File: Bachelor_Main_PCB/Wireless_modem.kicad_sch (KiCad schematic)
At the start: 59 parts, among them J13 CONMHF1-SMD-G-T, J14 CONMHF1-SMD-G-T, J21 CONMHF1-SMD-G-T, J25 M20-9990245, P1 SF70S006VBAR2000, Q10 NX3008NBKW, Q11 SSM3J358R,LF, Q12 NX3008NBKW, Q5 NX3008NBKW, Q6 NX3008NBKW, Q7 NX3008NBKW, Q8 NX3008NBKW, Q9 NX3008NBKW, U6 ESD7004MUTAG, U7 RC7620_1104627

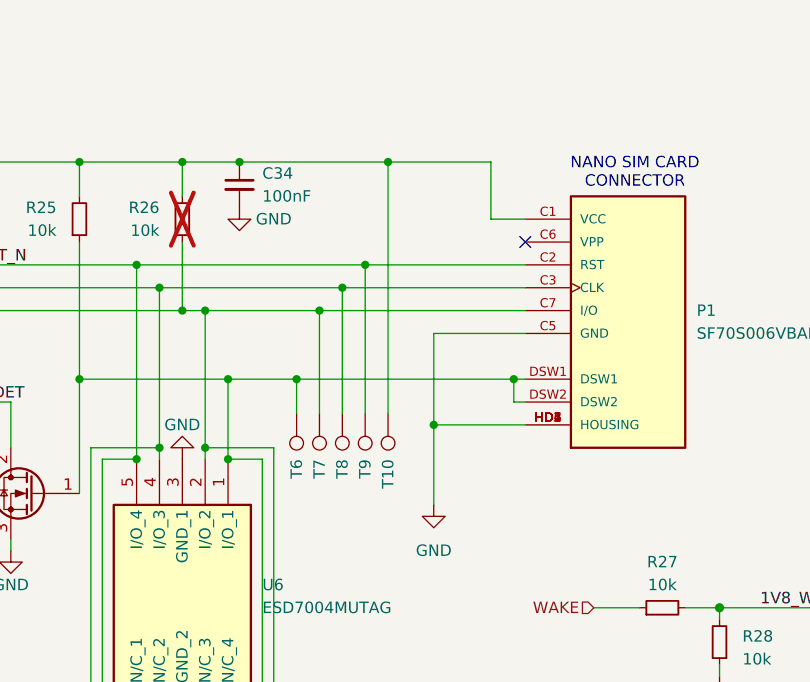
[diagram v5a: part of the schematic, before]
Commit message: arrange SIM card components. Fix DSW1 and DSW2 circuit.
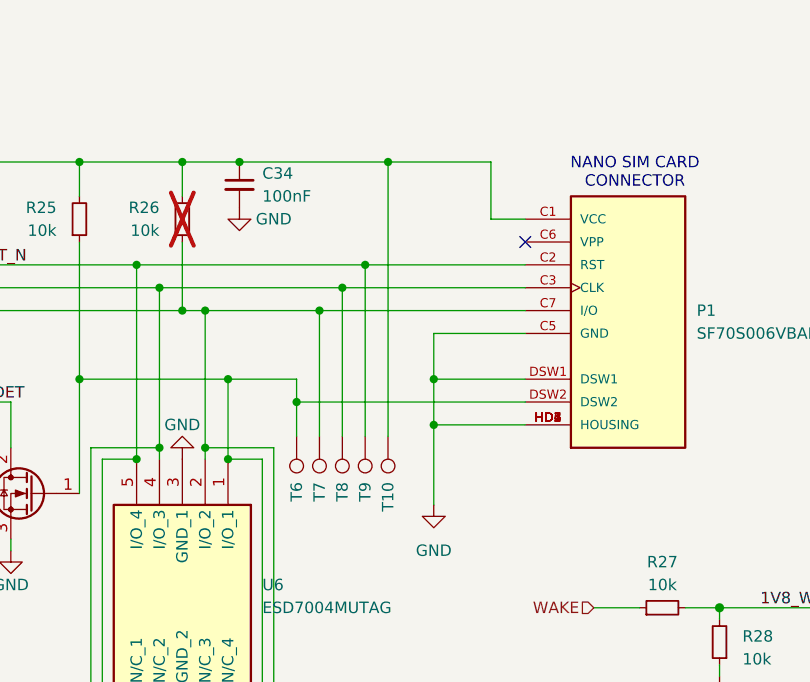
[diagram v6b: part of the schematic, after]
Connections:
- net GND: now also P1.DSW1
- net at P1.DSW2, Q5.1 (G), R25.1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: no longer P1.DSW1
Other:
- moved on the sheet: T10, T6, T7, T8, T9

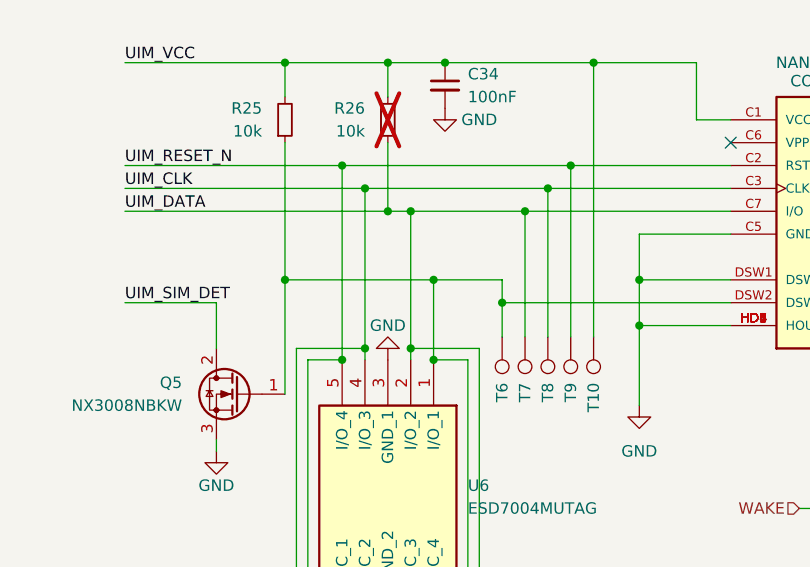
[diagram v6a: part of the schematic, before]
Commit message: arrange Modem mosfets
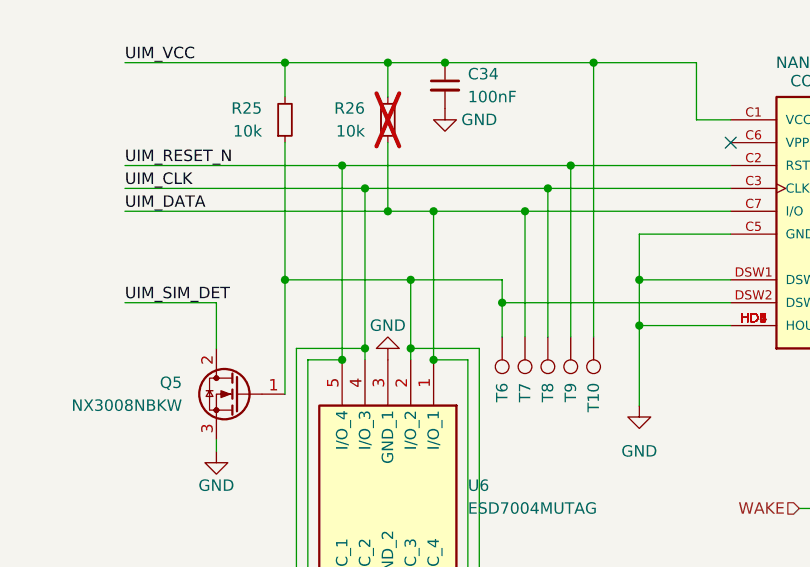
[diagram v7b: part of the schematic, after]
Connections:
- net UIM_DATA: now also U6.1 (I/O_1), U6.10 (N/C_4); no longer U6.2 (I/O_2), U6.9 (N/C_3)
- net at P1.DSW2, Q5.1 (G), R25.1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: now also U6.2 (I/O_2), U6.9 (N/C_3); no longer U6.1 (I/O_1), U6.10 (N/C_4)
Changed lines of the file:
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@@
+	)
+	(junction
+		(at 212.09 57.15)
+		(diameter 0)
+		(color 0 0 0 0)
 	)
 	(junction
@@
 	(junction
 		(at 68.58 168.91)
-		(diameter 0)
-		(color 0 0 0 0)
-	)
-	(junction
-		(at 212.09 49.53)
 		(diameter 0)
 		(color 0 0 0 0)
@@
 	)
 	(junction
-		(at 212.09 64.77)
-		(diameter 0)
-		(color 0 0 0 0)
-	)
-	(junction
 		(at 222.25 59.69)
 		(diameter 0)
@@
 	)
 	(junction
+		(at 214.63 66.04)
+		(diameter 0)
+		(color 0 0 0 0)
+	)
+	(junction
+		(at 212.09 64.77)
+		(diameter 0)
+		(color 0 0 0 0)
+	)
+	(junction
 		(at 207.01 64.77)
 		(diameter 0)
@@
 	)
 	(junction
-		(at 214.63 57.15)
-		(diameter 0)
-		(color 0 0 0 0)
-	)
-	(junction
 		(at 204.47 44.45)
 		(diameter 0)
@@
 	(junction
 		(at 123.19 189.23)
+		(diameter 0)
+		(color 0 0 0 0)
+	)
+	(junction
+		(at 214.63 49.53)
 		(diameter 0)
 		(color 0 0 0 0)
@@
 	)
 	(junction
-		(at 214.63 66.04)
-		(diameter 0)
-		(color 0 0 0 0)
-	)
-	(junction
 		(at 50.8 158.75)
 		(diameter 0)
@@
 	(wire
 		(pts
+			(xy 214.63 49.53) (xy 224.79 49.53)
+		)
+		(stroke
+			(width 0)
+			(type default)
+		)
+	)
+	(wire
+		(pts
 			(xy 243.84 39.37) (xy 247.65 39.37)
 		)
@@
 	(wire
 		(pts
-			(xy 214.63 57.15) (xy 198.12 57.15)
+			(xy 198.12 57.15) (xy 212.09 57.15)
 		)
 		(stroke
@@
 	(wire
 		(pts
+			(xy 212.09 57.15) (xy 212.09 64.77)
+		)
+		(stroke
+			(width 0)
+			(type default)
+		)
+	)
+	(wire
+		(pts
 			(xy 193.04 163.83) (xy 193.04 162.56)
 		)
@@
 	(wire
 		(pts
-			(xy 212.09 49.53) (xy 224.79 49.53)
-		)
-		(stroke
-			(width 0)
-			(type default)
-		)
-	)
-	(wire
-		(pts
 			(xy 143.51 182.88) (xy 143.51 181.61)
 		)
@@
 	(wire
 		(pts
-			(xy 214.63 57.15) (xy 214.63 66.04)
-		)
-		(stroke
-			(width 0)
-			(type default)
-		)
-	)
-	(wire
-		(pts
 			(xy 158.75 74.93) (xy 143.51 74.93)
 		)
@@
 	(wire
 		(pts
-			(xy 212.09 49.53) (xy 212.09 64.77)
-		)
-		(stroke
-			(width 0)
-			(type default)
-		)
-	)
-	(wire
-		(pts
 			(xy 193.04 129.54) (xy 193.04 130.81)
 		)
@@
 	(wire
 		(pts
-			(xy 222.25 57.15) (xy 214.63 57.15)
-		)
-		(stroke
-			(width 0)
-			(type default)
-		)
-	)
-	(wire
-		(pts
 			(xy 229.87 44.45) (xy 204.47 44.45)
 		)
@@
 	(wire
 		(pts
+			(xy 212.09 57.15) (xy 222.25 57.15)
+		)
+		(stroke
+			(width 0)
+			(type default)
+		)
+	)
+	(wire
+		(pts
 			(xy 123.19 186.69) (xy 123.19 189.23)
 		)
@@
 	(wire
 		(pts
-			(xy 209.55 49.53) (xy 212.09 49.53)
+			(xy 209.55 49.53) (xy 214.63 49.53)
 		)
 		(stroke
@@
 		)
 		(stroke
+			(width 0)
+			(type default)
+		)
+	)
+	(wire
+		(pts
+			(xy 214.63 49.53) (xy 214.63 66.04)
+		)
+		(stroke

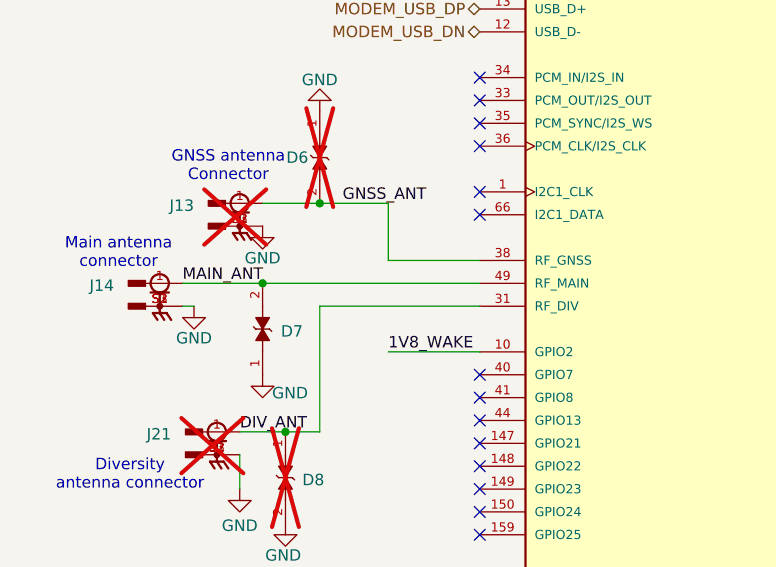
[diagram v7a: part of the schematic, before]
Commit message: Add custom nettie for Waveguide. Aligned modem connectors
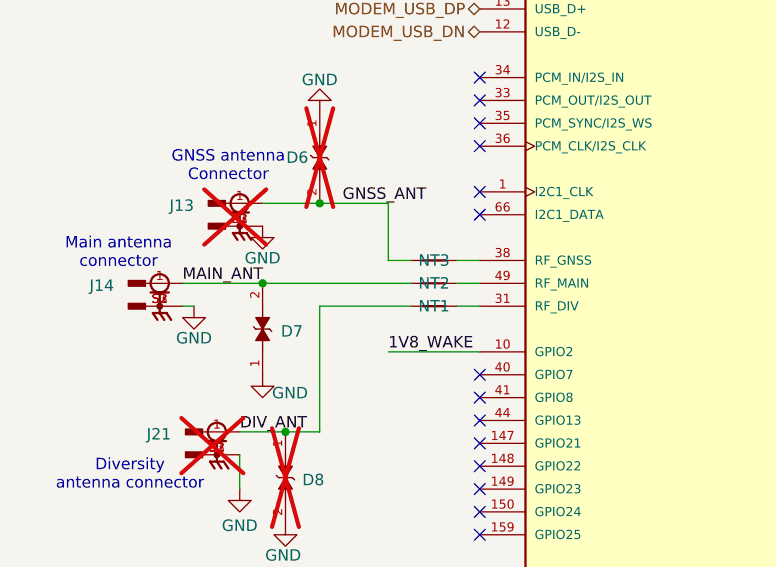
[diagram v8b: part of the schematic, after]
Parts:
- added NT1, NT2, NT3: NetTie_2, Net_tie_footprint_Waveguide_transmissionline:0.3mm_to_0.41_net_tie, symbol Device:NetTie_2
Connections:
- net DIV_ANT: now also NT1.1; no longer U7.31 (RF_DIV)
- net GNSS_ANT: now also NT3.1; no longer U7.38 (RF_GNSS)
- net MAIN_ANT: now also NT2.1; no longer U7.49 (RF_MAIN)
- new net: NT1.2, U7.31 (RF_DIV)
- new net: NT3.2, U7.38 (RF_GNSS)
- new net: NT2.2, U7.49 (RF_MAIN)
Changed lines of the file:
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@@
 	)
 	(junction
-		(at 38.1 102.87)
-		(diameter 0)
-		(color 0 0 0 0)
-	)
-	(junction
 		(at 237.49 62.23)
 		(diameter 0)
@@
 	)
 	(junction
+		(at 38.1 102.87)
+		(diameter 0)
+		(color 0 0 0 0)
+	)
+	(junction
 		(at 181.61 135.89)
 		(diameter 1.016)
@@
 	(wire
 		(pts
+			(xy 59.69 105.41) (xy 62.23 105.41)
+		)
+		(stroke
+			(width 0)
+			(type default)
+		)
+	)
+	(wire
+		(pts
 			(xy 123.19 184.15) (xy 123.19 186.69)
 		)
@@
 	(wire
 		(pts
-			(xy 144.78 115.57) (xy 143.51 115.57)
+			(xy 59.69 102.87) (xy 62.23 102.87)
+		)
+		(stroke
+			(width 0)
+			(type default)
+		)
+	)
+	(wire
+		(pts
+			(xy 38.1 102.87) (xy 54.61 102.87)
 		)
 		(stroke
@@
 	(wire
 		(pts
-			(xy 38.1 102.87) (xy 62.23 102.87)
+			(xy 144.78 115.57) (xy 143.51 115.57)
 		)
 		(stroke
@@
 	(wire
 		(pts
-			(xy 44.45 105.41) (xy 62.23 105.41)
-		)
-		(stroke
-			(width 0)
-			(type default)
-		)
-	)
-	(wire
-		(pts
 			(xy 212.09 97.79) (xy 219.71 97.79)
 		)
@@
 	(wire
 		(pts
+			(xy 44.45 105.41) (xy 54.61 105.41)
+		)
+		(stroke
+			(width 0)
+			(type default)
+		)
+	)
+	(wire
+		(pts
 			(xy 81.28 189.23) (xy 81.28 190.5)
 		)
@@
 	(wire
 		(pts
+			(xy 59.69 100.33) (xy 62.23 100.33)
+		)
+		(stroke
+			(width 0)
+			(type default)
+		)
+	)
+	(wire
+		(pts
 			(xy 128.27 182.88) (xy 128.27 181.61)
 		)
@@
 	(wire
 		(pts
-			(xy 50.8 158.75) (xy 50.8 163.83)
+			(xy 52.07 100.33) (xy 54.61 100.33)
 		)
 		(stroke
@@
 	(wire
 		(pts
-			(xy 158.75 67.31) (xy 144.78 67.31)
+			(xy 50.8 158.75) (xy 50.8 163.83)
 		)
 		(stroke
@@
 	(wire
 		(pts
-			(xy 204.47 96.52) (xy 200.66 96.52)
+			(xy 158.75 67.31) (xy 144.78 67.31)
 		)
 		(stroke
@@
 	(wire
 		(pts
-			(xy 190.5 59.69) (xy 190.5 64.77)
+			(xy 204.47 96.52) (xy 200.66 96.52)
 		)
 		(stroke
@@
 	(wire
 		(pts
-			(xy 209.55 49.53) (xy 214.63 49.53)
+			(xy 190.5 59.69) (xy 190.5 64.77)
 		)
 		(stroke
@@
 	(wire
 		(pts
-			(xy 52.07 100.33) (xy 62.23 100.33)
+			(xy 209.55 49.53) (xy 214.63 49.53)
 		)
 		(stroke
@@
 	)
 	(symbol
+		(lib_id "Device:NetTie_2")
+		(at 57.15 102.87 0)
+		(unit 1)
+		(exclude_from_sim no)
+		(in_bom no)
+		(on_board yes)
+		(dnp no)
+		(property "Reference" "NT2"
+			(at 57.15 102.87 0)
+			(effects
+				(font
+					(size 1.27 1.27)
+				)
+			)
+		)
+		(property "Value" "NetTie_2"
+			(at 57.15 100.33 0)
+			(effects
+				(font
+					(size 1.27 1.27)
+				)
+				(hide yes)
+			)
+		)
+		(property "Footprint" "Net_tie_footprint_Waveguide_transmissionline:0.3mm_to_0.41_net_tie"
+			(at 57.15 102.87 0)
+			(effects
+				(font
+					(size 1.27 1.27)
+				)
+				(hide yes)
+			)
+		)
+		(property "Datasheet" "~"
+			(at 57.15 102.87 0)
+			(effects
+				(font
+					(size 1.27 1.27)
+				)
+				(hide yes)
+			)
+		)
+		(property "Description" "Net tie, 2 pins"
+			(at 57.15 102.87 0)
+			(effects
+				(font
+					(size 1.27 1.27)
+				)
+				(hide yes)
+			)
+		)
+		(pin "1"
+		)
+		(pin "2"
+		)
+		(instances
+			(project "Bachelor_Main_PCB"
+				(path "/3544d663-329e-4884-b753-28436ca187e8/0bbef2a3-1d79-4cf0-b531-d6abf690b331"
+					(reference "NT2")
+					(unit 1)
+				)
+			)
+		)
+	)
+	(symbol
 		(lib_id "CONMHF1-SMD-G-T:CONMHF1-SMD-G-T")
 		(at 35.56 93.98 0)
@@
 	)
 	(symbol
+		(lib_id "Device:NetTie_2")
+		(at 57.15 105.41 0)
+		(unit 1)
+		(exclude_from_sim no)
+		(in_bom no)
+		(on_board yes)
+		(dnp no)
+		(property "Reference" "NT1"
+			(at 57.15 105.41 0)
+			(effects
+				(font
+					(size 1.27 1.27)
+				)
+			)
+		)
+		(property "Value" "NetTie_2"
+			(at 57.15 102.87 0)
+			(effects
+				(font
+					(size 1.27 1.27)
+				)
+				(hide yes)
+			)
+		)
+		(property "Footprint" "Net_tie_footprint_Waveguide_transmissionline:0.3mm_to_0.41_net_tie"
+			(at 57.15 105.41 0)
+			(effects
+				(font
+					(size 1.27 1.27)
+				)
+				(hide yes)
+			)
+		)
+		(property "Datasheet" "~"
+			(at 57.15 105.41 0)
+			(effects
+				(font
+					(size 1.27 1.27)
+				)
+				(hide yes)
+			)
+		)
+		(property "Description" "Net tie, 2 pins"
+			(at 57.15 105.41 0)
+			(effects
+				(font
+					(size 1.27 1.27)
+				)
+				(hide yes)
+			)
+		)
+		(pin "1"
+		)
+		(pin "2"
+		)
+		(instances
+			(project "Bachelor_Main_PCB"
+				(path "/3544d663-329e-4884-b753-28436ca187e8/0bbef2a3-1d79-4cf0-b531-d6abf690b331"
+					(reference "NT1")
+					(unit 1)
+				)
+			)
+		)
+	)
+	(symbol
 		(lib_id "power:GND")
 		(at 243.84 118.11 0)
@@
 					(unit 1)
 				)
+			)
+		)
+	)
+	(symbol
+		(lib_id "Device:NetTie_2")
+		(at 57.15 100.33 0)
+		(unit 1)
+		(exclude_from_sim no)
+		(in_bom no)
+		(on_board yes)
+		(dnp no)
+		(property "Reference" "NT3"
+			(at 57.15 100.33 0)
+			(effects
+				(font
+					(size 1.27 1.27)
+				)
+			)
+		)
+		(property "Value" "NetTie_2"
+			(at 57.15 97.79 0)
+			(effects
+				(font
+					(size 1.27 1.27)
+				)
+				(hide yes)
+			)
+		)
+		(property "Footprint" "Net_tie_footprint_Waveguide_transmissionline:0.3mm_to_0.41_net_tie"
+			(at 57.15 100.33 0)
+			(effects
+				(font
+					(size 1.27 1.27)
+				)
+				(hide yes)
+			)
+		)
+		(property "Datasheet" "~"
+			(at 57.15 100.33 0)
+			(effects
+				(font
+					(size 1.27 1.27)
+				)
+				(hide yes)
+			)
+		)
+		(property "Description" "Net tie, 2 pins"
+			(at 57.15 100.33 0)
+			(effects
+				(font
+					(size 1.27 1.27)
+				)
+				(hide yes)
+			)
+		)
+		(pin "1"
+		)
+		(pin "2"
+		)
+		(instances
+			(project "Bachelor_Main_PCB"
+				(path "/3544d663-329e-4884-b753-28436ca187e8/0bbef2a3-1d79-4cf0-b531-d6abf690b331"
+					(reference "NT3")
+					(unit 1)
+				)
